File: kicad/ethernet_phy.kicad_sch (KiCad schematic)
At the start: 37 parts, among them U7 TJA1103AHN, Y1 25MHz

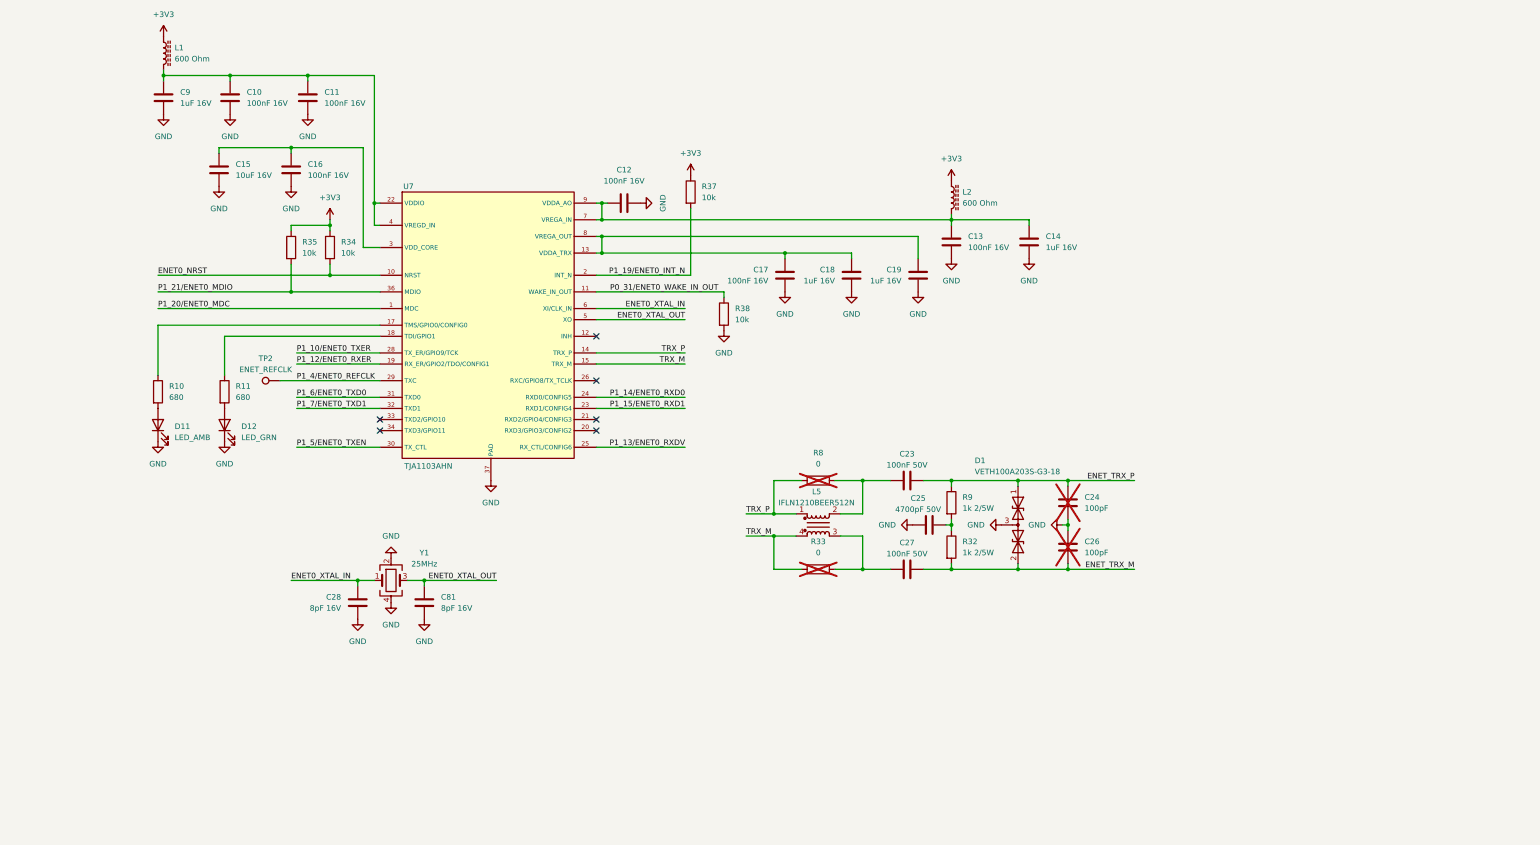
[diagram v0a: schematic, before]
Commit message: Updated schematic and started on layout
- Implemented schematic changes after feedback:
	- BMM350 VDD is 1.8V
	- Replaced net labels with global labels for page references
	- Added 1uF cap to SK9822-EC20
- Added rev-RMII configuration for TJA1103 and DNP resistor to put it in slave mode
- Added TJA1103 PHY address info
- Changed decoupling caps for MCXN to smallest possible packages
- Added traces and vias at MCXN according to guidelines
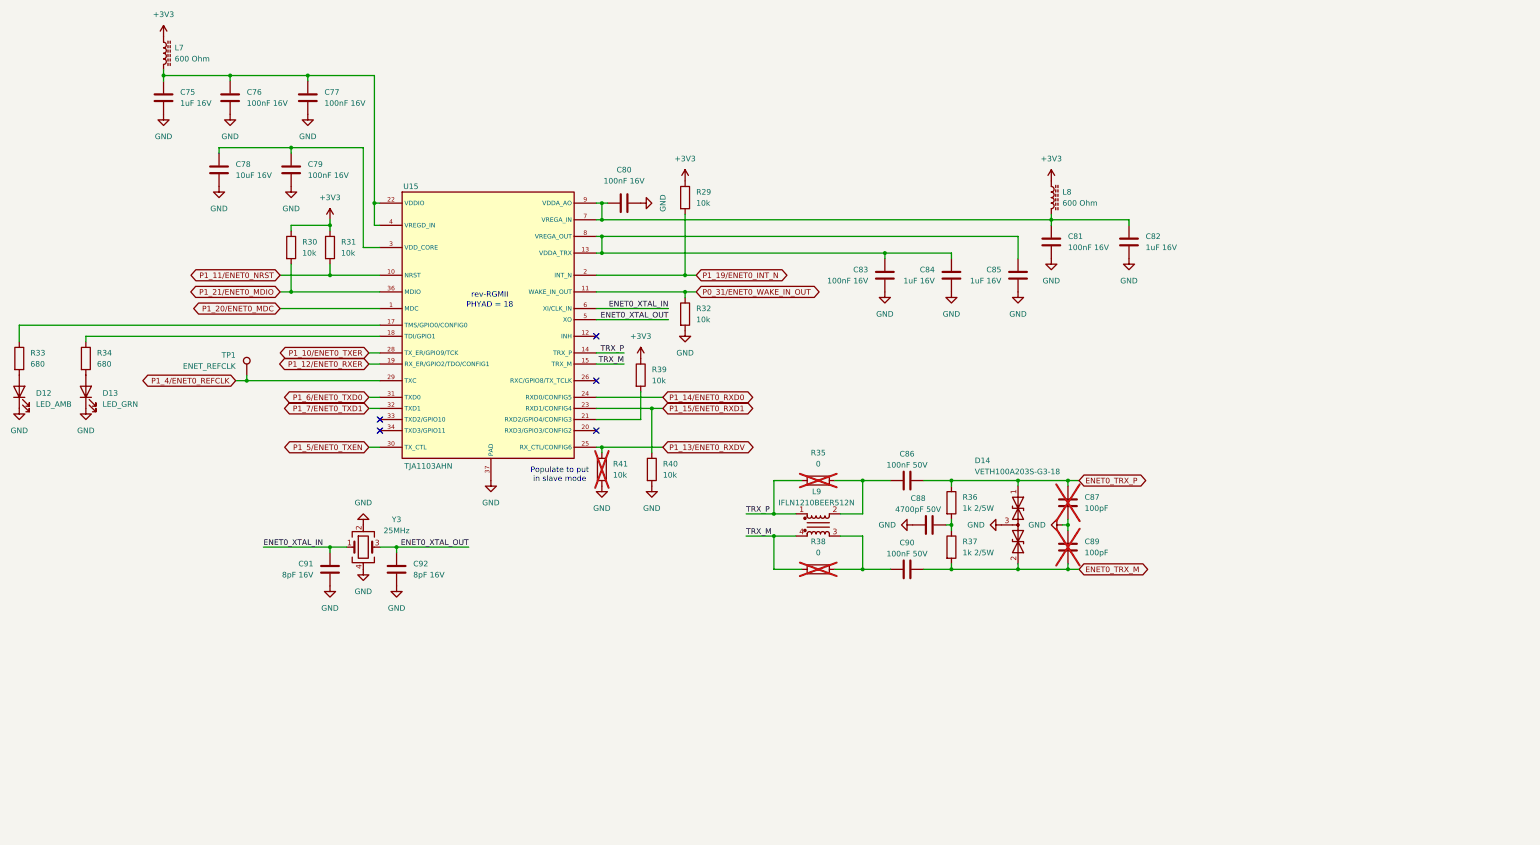
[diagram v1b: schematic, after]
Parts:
- added R39, R40, R41: 10k, Resistor_SMD:R_0402_1005Metric, symbol Device:R
- renumbered C9 to C75, C10 to C76, C11 to C77, C15 to C78, C16 to C79, C12 to C80, C13 to C81, C14 to C82, C17 to C83, C18 to C84, C19 to C85, C23 to C86, C24 to C87, C25 to C88, C26 to C89, C27 to C90, C28 to C91, C81 to C92, D11 to D12, D12 to D13, D1 to D14, L1 to L7, L2 to L8, L5 to L9, R37 to R29, R35 to R30, R34 to R31, R38 to R32, R10 to R33, R11 to R34, R8 to R35, R9 to R36, R32 to R37, R33 to R38, TP2 to TP1, U7 to U15, Y1 to Y3
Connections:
- net +3V3: now also R39.1
- net GND: now also R40.2, R41.2
- net P1_13/ENET0_RXDV: now also R41.1
- net P1_15/ENET0_RXD1: now also R40.1
- net at U15.21 (RXD2/GPIO4/CONFIG3): now also R39.2
- net ENET0_NRST renamed P1_11/ENET0_NRST
- net ENET_TRX_M renamed ENET0_TRX_M
- net ENET_TRX_P renamed ENET0_TRX_P
- no-connect marks 6 -> 5
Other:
- note added: "PHYAD = 18"
- note added: "Populate to put in slave mode"
- note added: "rev-RGMII"
- moved on the sheet: C81, C82, C83, C84, C85, C91, C92, D12, D13, L8, R29, R32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

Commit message: Updated schematic after feedback from Jari
- Finished schematic after feedback from Jari. It is at a finished state, can be reviewed by whole team now.
- Layouted MCXN with decoupling caps.
- Layouted Base100-T1 ethernet phy.
- Layouted the power supply a bit.
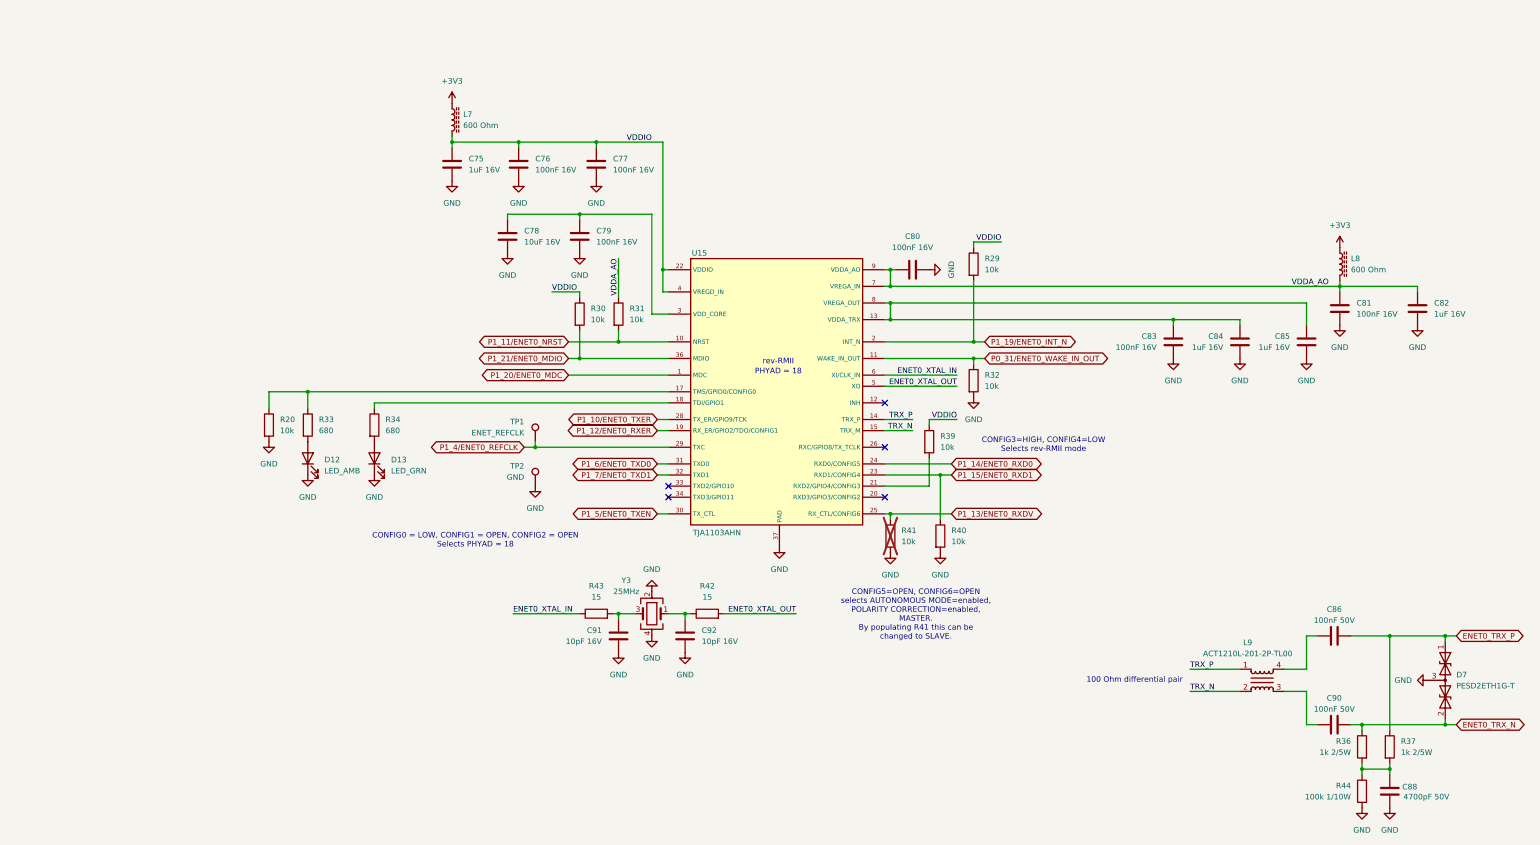
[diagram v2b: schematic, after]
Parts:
- removed C87, C89: 100pF, Capacitor_SMD:C_0402_1005Metric, symbol Device:C
- removed D14: VETH100A203S-G3-18, Package_TO_SOT_SMD:SOT-23, symbol Diodes:VETH100A203S-G3-18
- removed L9: IFLN1210BEER512N, Inductors:IFLN1210BEER512N, symbol Inductors:IFLN1210BEER512N
- removed R35, R38: 0, Resistor_SMD:R_0402_1005Metric, symbol Device:R
- added D7: PESD2ETH1G-T, Package_TO_SOT_SMD:SOT-23, symbol Diodes:PESD2ETH1G-T
- added L9: ACT1210L-201-2P-TL00, Inductors:ACT1210L1012PTL00, symbol Inductors:ACT1210L-201-2P-TL00
- added R20: 10k, Resistor_SMD:R_0402_1005Metric, symbol Device:R
- added R42, R43: 15, Resistor_SMD:R_0402_1005Metric, symbol Device:R
- added R44: 100k 1/10W, Resistor_SMD:R_0402_1005Metric, symbol Device:R
- added TP2: GND, TestPoint:TestPoint_Pad_D1.0mm, symbol Connector:TestPoint
- C91, C92: value 8pF 16V -> 10pF 16V; MFPN GCM1555C1H8R0DA16D -> GRM1555C1H100JA01D; Supplier PN C126517 -> C76946
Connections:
- net +3V3: no longer R29.1, R30.1, R31.1, R39.1
- net ENET0_TRX_P: now also R37.1, D7.1 (A1); no longer R36.1
- net ENET0_XTAL_IN: now also R43.1; no longer C91.1, Y3.1
- net ENET0_XTAL_OUT: now also R42.2; no longer C92.1, Y3.3
- net GND: now also C88.2, D7.3 (common), R20.2, R44.2, TP2.1; no longer C88.1
- net TRX_P: now also L9.1
- net VDDIO: now also R29.1, R30.1, R39.1
- net VDDA_AO: now reaches C80.1, C81.2, C82.2, L8.2, U15.7 (VREGA_IN), U15.9 (VDDA_AO)
- net VDDA_AO: now also R31.1
- net at R33.1, U15.17 (TMS/GPIO0/CONFIG0): now also R20.1
- net at C90.1: now also L9.3
- net at C86.1: now also L9.4
- net ENET0_TRX_M: no longer names the net of R37.2
- net ENET0_TRX_M: now also C88.1, R36.2, R44.1; no longer C90.2
- net TRX_M renamed TRX_N
- net TRX_N: now also L9.2
- new net: C92.1, R42.1, Y3.1
- new net: C91.1, R43.2, Y3.3
- new net ENET0_TRX_N: C90.2, D7.2 (A2), R36.1
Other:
- note added: "100 Ohm differential pair"
- note added: "CONFIG0 = LOW, CONFIG1 = OPEN, CONFIG2 = OPEN Selects PHYAD = 18"
- note added: "CONFIG3=HIGH, CONFIG4=LOW Selects rev-RMII mode"
- note added: "CONFIG5=OPEN, CONFIG6=OPEN selects AUTONOMOUS MODE=enabled, POLARITY CORRECTION=enabled, MASTER. By populating R41 this can be changed to SLAVE."
- note added: "rev-RMII"
- note removed: "Populate to put in slave mode"
- note removed: "rev-RGMII"
- title: MR-MCXN-T1 Sensor hub -> MR-MCXN-T1 Sensor Node
- moved on the sheet: C75, C76, C77, C78, C79, C80, C81, C82, C83, C84, C85, C86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

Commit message: Finished schematic. Completed power and ENET phy layout.
Layouted power supply and ethernet phy around input connector.
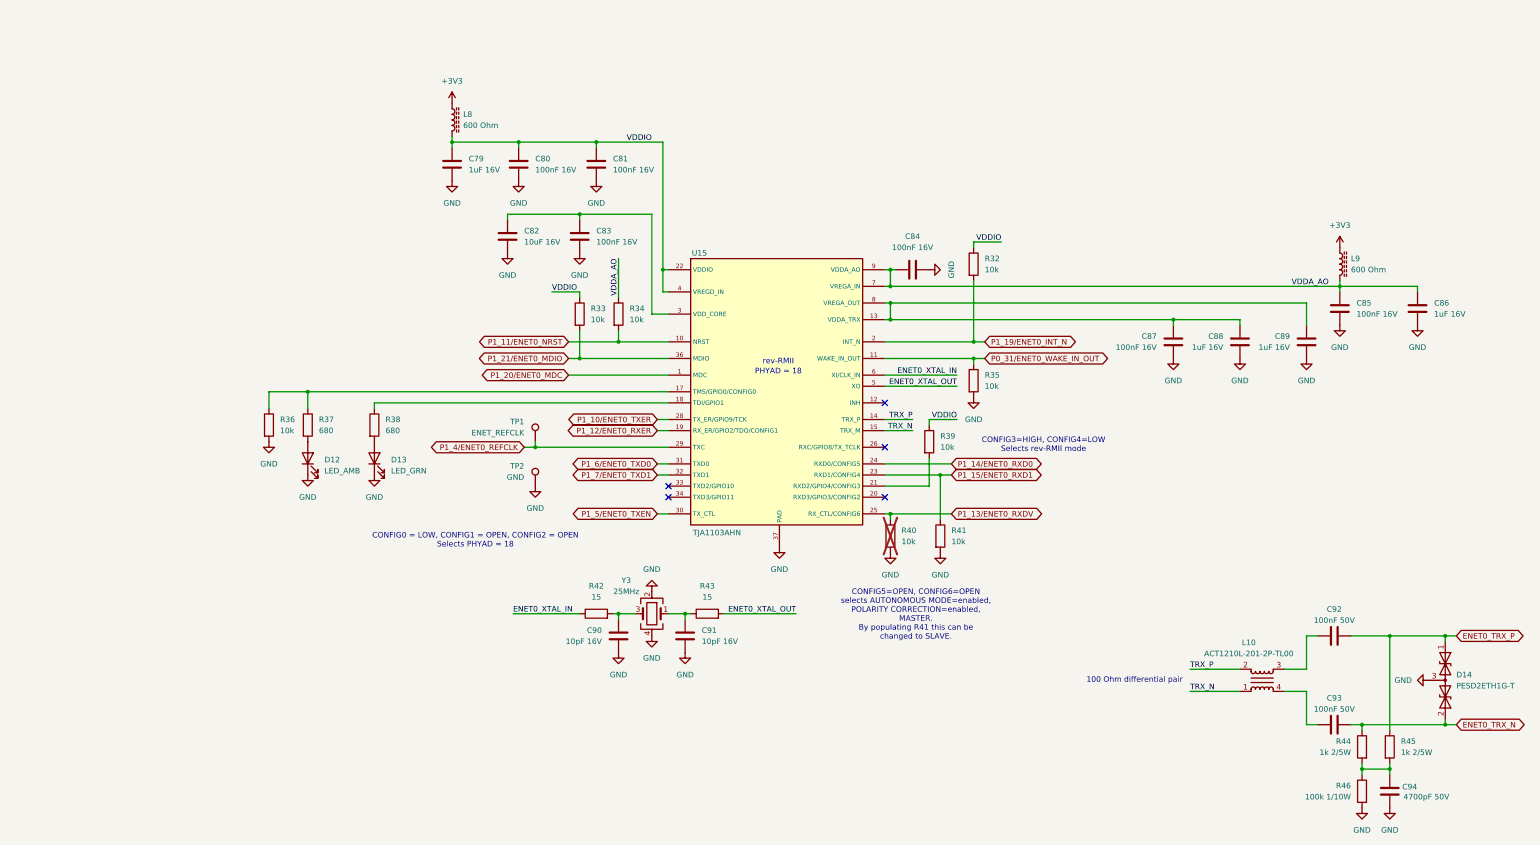
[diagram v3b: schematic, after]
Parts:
- D14: renamed from D7; MF (none) -> Nexperia; MFPN (none) -> PESD2ETH1G-TR; Supplier (none) -> JLCPCB; Supplier PN (none) -> C2594873
- renumbered C75 to C79, C76 to C80, C77 to C81, C78 to C82, C79 to C83, C80 to C84, C81 to C85, C82 to C86, C83 to C87, C84 to C88, C85 to C89, C91 to C90, C92 to C91, C86 to C92, C90 to C93, C88 to C94, L9 to L10, L7 to L8, L8 to L9, R29 to R32, R30 to R33, R31 to R34, R32 to R35, R20 to R36, R33 to R37, R34 to R38, R41 to R40, R40 to R41, R43 to R42, R42 to R43, R36 to R44, R37 to R45, R44 to R46
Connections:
- net TRX_N: now also L10.1; no longer L10.2
- net TRX_P: now also L10.2; no longer L10.1
- net at C92.1: now also L10.3; no longer L10.4
- net at C93.1: now also L10.4; no longer L10.3

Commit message: Updated layout and BOM
- Rounded corners of PCB
- Updated board-to-board MFPN to correct one.
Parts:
- TP1, TP2: now left out of the parts list
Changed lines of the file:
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@@
 		(unit 1)
 		(exclude_from_sim no)
-		(in_bom yes)
+		(in_bom no)
 		(on_board yes)
 		(dnp no)
@@
 		(unit 1)
 		(exclude_from_sim no)
-		(in_bom yes)
+		(in_bom no)
 		(on_board yes)
 		(dnp no)

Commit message: Updated layout and BOM
- Flipped Magnetometer so it is aligned with the axis of the IMU.
- Updated BOM so all parts can be sourced from DigiKey. Also added a row for JLCPCB part numbers if applicable.
- Replaced ISP button with the NanoT160AS. Added "ISP" in silkscreen at that button.
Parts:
- C79, C86, C88, C89: DigiKey (none) -> 490-5241-1-ND; JLCPCB (none) -> C161212; MF Samsung Electro-Mechanics -> Murata Electronics; MFPN CL10B105KO8NNNC -> GCM188R71C105KA64D; Supplier JLCPCB -> (none); Supplier PN C59782 -> (none)
- C80, C81, C83, C84, C85, C87: DigiKey (none) -> 490-3261-1-ND; JLCPCB (none) -> C71629; MF Samsung Electro-Mechanics -> Murata Electronics; MFPN CL05B104KO5NNNC -> GRM155R71C104KA88D; Supplier JLCPCB -> (none); Supplier PN C1525 -> (none)
- C82: DigiKey (none) -> 490-GRM21BZ71C106KE15LCT-ND; JLCPCB (none) -> C162430; MF Samsung Electro-Mechanics -> Murata Electronics; MFPN CL21B106KOQNNNE -> GRM21BZ71C106KE15L; Supplier JLCPCB -> (none); Supplier PN C95841 -> (none)
- C90, C91: DigiKey (none) -> 490-5921-1-ND; JLCPCB (none) -> C76946; Supplier JLCPCB -> (none); Supplier PN C76946 -> (none)
- C92, C93: DigiKey (none) -> 490-10700-1-ND; JLCPCB (none) -> C77020; Supplier JLCPCB -> (none); Supplier PN C77020 -> (none)
- C94: DigiKey (none) -> 311-1418-1-ND; JLCPCB (none) -> C106208; Supplier JLCPCB -> (none); Supplier PN C106208 -> (none)
- D12: DigiKey (none) -> 732-150060AS75000CT-ND; JLCPCB (none) -> C6976659; MF BrtLed(Bright LED Elec) -> Würth Elektronik; MFPN BL-HJC36G-AV-TRB -> 150060AS75000; Supplier JLCPCB -> (none); Supplier PN C165983 -> (none)
- D13: DigiKey (none) -> 754-1116-1-ND; JLCPCB (none) -> C5119770; MF Silverlight -> Kingbright; MFPN P0603P1N46G12 -> APT1608CGCK; Supplier JLCPCB -> (none); Supplier PN C5123548 -> (none)
- D14: DigiKey (none) -> 1727-PESD2ETH1G-CT-ND; JLCPCB (none) -> C2594873; Supplier JLCPCB -> (none); Supplier PN C2594873 -> (none)
- L10: DigiKey (none) -> 445-ACT1210L-201-2P-TL00CT-ND; JLCPCB (none) -> -; MF TDK -> TDK Corporation; Supplier Mouser -> (none); Supplier PN 810-ACT1210L-2012P00 -> (none)
- L8, L9: DigiKey (none) -> 490-1006-1-ND; JLCPCB (none) -> C76884; Supplier JLCPCB -> (none); Supplier PN C76884 -> (none)
- R32, R33, R34, R35, R36, R39, R41: DigiKey (none) -> YAG3436CT-ND; JLCPCB (none) -> C144807; MF UNI-ROYAL(Uniroyal Elec) -> YAGEO; MFPN 0402WGF1002TCE -> AC0402FR-0710KL; Supplier JLCPCB -> (none); Supplier PN C25744 -> (none)
- R37, R38: footprint Inductor_SMD:L_0402_1005Metric -> Resistor_SMD:R_0402_1005Metric; DigiKey (none) -> YAG3505CT-ND; JLCPCB (none) -> C227187; MF UNI-ROYAL(Uniroyal Elec) -> YAGEO; MFPN 0402WGF6800TCE -> AC0402FR-07680RL; Supplier JLCPCB -> (none); Supplier PN C25130 -> (none)
- R40: Supplier JLCPCB -> (none); Supplier PN C25744 -> (none)
- R42, R43: DigiKey (none) -> YAG3445CT-ND; JLCPCB (none) -> C226797; MF UNI-ROYAL(Uniroyal Elec) -> YAGEO; MFPN 0402WGF150JTCE -> AC0402FR-0715RL; Supplier JLCPCB -> (none); Supplier PN C25083 -> (none)
- R44, R45: DigiKey (none) -> RHM1.00KAECT-ND; JLCPCB (none) -> -; Supplier DigiKey -> (none); Supplier PN RHM1.00KAECT-ND -> (none)
- R46: DigiKey (none) -> 13-RC0402FR-7W100KLCT-ND; JLCPCB (none) -> C606167; Supplier JLCPCB -> (none); Supplier PN C606167 -> (none)
- U15: DigiKey (none) -> 568-TJA1103AHN/0ZCT-ND; JLCPCB (none) -> -; Supplier DigiKey -> (none); Supplier PN 568-TJA1103AHN/0ZCT-ND -> (none)
- Y3: DigiKey (none) -> 490-12146-1-ND; JLCPCB (none) -> -; Supplier DigiKey -> (none); Supplier PN 490-12146-1-ND -> (none)

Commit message: Update repo naming and cleanup files.
Signed-off-by: Benjamin Perseghetti <bperseghetti@rudislabs.com>
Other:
- title: MR-MCXN-T1 Sensor Node -> MR-MCXN-T1

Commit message: Patched schematic and board layout
- Replaced choke in series with Vbus with 2A choke.
- Fixed interface to the BMP581 barometer.
- Added schematic fixes to the layout.
- Completed DRC.
- Created production folder with Gerber, BOM, positions and schematic.
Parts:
- R40: DigiKey (none) -> YAG3436CT-ND; JLCPCB (none) -> C144807; MF UNI-ROYAL(Uniroyal Elec) -> YAGEO; MFPN 0402WGF1002TCE -> AC0402FR-0710KL
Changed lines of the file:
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@@
 (kicad_sch
-	(version 20231120)
+	(version 20250114)
 	(generator "eeschema")
-	(generator_version "8.0")
+	(generator_version "9.0")
 	(paper "A3")
 	(title_block
@@
 		(comment 4 "CTO SYSTEM INNOVATIONS / MOBILE ROBOTICS DOMAIN")
 	)
+	(text "CONFIG0 = LOW, CONFIG1 = OPEN, CONFIG2 = OPEN \nSelects PHYAD = 18"
+		(exclude_from_sim no)
+		(at 125.984 147.066 0)
+		(effects
+			(font
+				(size 1.27 1.27)
+			)
+		)
+	)
+	(text "100 Ohm differential pair"
+		(exclude_from_sim no)
+		(at 276.86 179.07 0)
+		(effects
+			(font
+				(size 1.27 1.27)
+			)
+		)
+	)
+	(text "rev-RMII"
+		(exclude_from_sim no)
+		(at 195.326 106.172 0)
+		(effects
+			(font
+				(size 1.27 1.27)
+			)
+		)
+	)
+	(text "PHYAD = 18"
+		(exclude_from_sim no)
+		(at 195.326 108.458 0)
+		(effects
+			(font
+				(size 1.27 1.27)
+			)
+		)
+	)
+	(text "CONFIG5=OPEN, CONFIG6=OPEN \nselects AUTONOMOUS MODE=enabled, \nPOLARITY CORRECTION=enabled, \nMASTER. \nBy populating R41 this can be \nchanged to SLAVE."
+		(exclude_from_sim no)
+		(at 226.822 164.084 0)
+		(effects
+			(font
+				(size 1.27 1.27)
+			)
+		)
+	)
+	(text "CONFIG3=HIGH, CONFIG4=LOW \nSelects rev-RMII mode"
+		(exclude_from_sim no)
+		(at 256.032 125.222 0)
+		(effects
+			(font
+				(size 1.27 1.27)
+			)
+		)
+	)
 	(junction
 		(at 323.85 88.9)
@@
 		)
 	)
-	(text "CONFIG0 = LOW, CONFIG1 = OPEN, CONFIG2 = OPEN \nSelects PHYAD = 18"
-		(exclude_from_sim no)
-		(at 125.984 147.066 0)
-		(effects
-			(font
-				(size 1.27 1.27)
-			)
-		)
-	)
-	(text "100 Ohm differential pair"
-		(exclude_from_sim no)
-		(at 276.86 179.07 0)
-		(effects
-			(font
-				(size 1.27 1.27)
-			)
-		)
-	)
-	(text "rev-RMII"
-		(exclude_from_sim no)
-		(at 195.326 106.172 0)
-		(effects
-			(font
-				(size 1.27 1.27)
-			)
-		)
-	)
-	(text "PHYAD = 18"
-		(exclude_from_sim no)
-		(at 195.326 108.458 0)
-		(effects
-			(font
-				(size 1.27 1.27)
-			)
-		)
-	)
-	(text "CONFIG5=OPEN, CONFIG6=OPEN \nselects AUTONOMOUS MODE=enabled, \nPOLARITY CORRECTION=enabled, \nMASTER. \nBy populating R41 this can be \nchanged to SLAVE."
-		(exclude_from_sim no)
-		(at 226.822 164.084 0)
-		(effects
-			(font
-				(size 1.27 1.27)
-			)
-		)
-	)
-	(text "CONFIG3=HIGH, CONFIG4=LOW \nSelects rev-RMII mode"
-		(exclude_from_sim no)
-		(at 256.032 125.222 0)
-		(effects
-			(font
-				(size 1.27 1.27)
-			)
-		)
-	)
 	(label "VDDIO"
 		(at 143.51 90.17 0)
@@
 			)
 		)
-		(property "MF" "UNI-ROYAL(Uniroyal Elec)"
+		(property "MF" "YAGEO"
+			(at 220.98 146.05 0)
+			(effects
+				(font
+					(size 1.27 1.27)
+				)
+				(hide yes)
+			)
+		)
+		(property "MFPN" "AC0402FR-0710KL"
+			(at 220.98 146.05 0)
+			(effects
+				(font
+					(size 1.27 1.27)
+				)
+				(hide yes)
+			)
+		)
+		(property "DigiKey" "YAG3436CT-ND"
 			(at 220.98 146.05 0)
 			(effects
@@
 			)
 		)
-		(property "MFPN" "0402WGF1002TCE"
+		(property "JLCPCB" "C144807"
 			(at 220.98 146.05 0)
 			(effects
